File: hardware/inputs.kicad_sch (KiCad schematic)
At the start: 49 parts, among them J1 OLED_128x64

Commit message: fix switches to be correct order and move diodes
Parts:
- renumbered S15 to S13, S16 to S14, S17 to S15, S18 to S16, S13 to S17, S14 to S18
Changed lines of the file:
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@@
 		(dnp no)
 		(fields_autoplaced yes)
-		(property "Reference" "S14"
+		(property "Reference" "S18"
 			(at 220.98 62.23 0)
 			(effects
@@
 			(project "final_macropad"
 				(path "/5d184ef1-151a-4114-9d49-de87ac832ddf/ff01279d-20e0-401c-840f-7481298d2544"
-					(reference "S14")
+					(reference "S18")
 					(unit 1)
 				)
@@
 		(dnp no)
 		(fields_autoplaced yes)
-		(property "Reference" "S18"
+		(property "Reference" "S16"
 			(at 101.6 96.52 0)
 			(effects
@@
 			(project "final_macropad"
 				(path "/5d184ef1-151a-4114-9d49-de87ac832ddf/ff01279d-20e0-401c-840f-7481298d2544"
-					(reference "S18")
+					(reference "S16")
 					(unit 1)
 				)
@@
 		(dnp no)
 		(fields_autoplaced yes)
-		(property "Reference" "S15"
+		(property "Reference" "S13"
 			(at 62.23 96.52 0)
 			(effects
@@
 			(project "final_macropad"
 				(path "/5d184ef1-151a-4114-9d49-de87ac832ddf/ff01279d-20e0-401c-840f-7481298d2544"
-					(reference "S15")
+					(reference "S13")
 					(unit 1)
 				)
@@
 		(dnp no)
 		(fields_autoplaced yes)
-		(property "Reference" "S13"
+		(property "Reference" "S17"
 			(at 220.98 29.21 0)
 			(effects
@@
 			(project "final_macropad"
 				(path "/5d184ef1-151a-4114-9d49-de87ac832ddf/ff01279d-20e0-401c-840f-7481298d2544"
-					(reference "S13")
+					(reference "S17")
 					(unit 1)
 				)
@@
 		(dnp no)
 		(fields_autoplaced yes)
-		(property "Reference" "S17"
+		(property "Reference" "S15"
 			(at 87.63 96.52 0)
 			(effects
@@
 			(project "final_macropad"
 				(path "/5d184ef1-151a-4114-9d49-de87ac832ddf/ff01279d-20e0-401c-840f-7481298d2544"
-					(reference "S17")
+					(reference "S15")
 					(unit 1)
 				)
@@
 		(dnp no)
 		(fields_autoplaced yes)
-		(property "Reference" "S16"
+		(property "Reference" "S14"
 			(at 76.2 96.52 0)
 			(effects
@@
 			(project "final_macropad"
 				(path "/5d184ef1-151a-4114-9d49-de87ac832ddf/ff01279d-20e0-401c-840f-7481298d2544"
-					(reference "S16")
+					(reference "S14")
 					(unit 1)
 				)

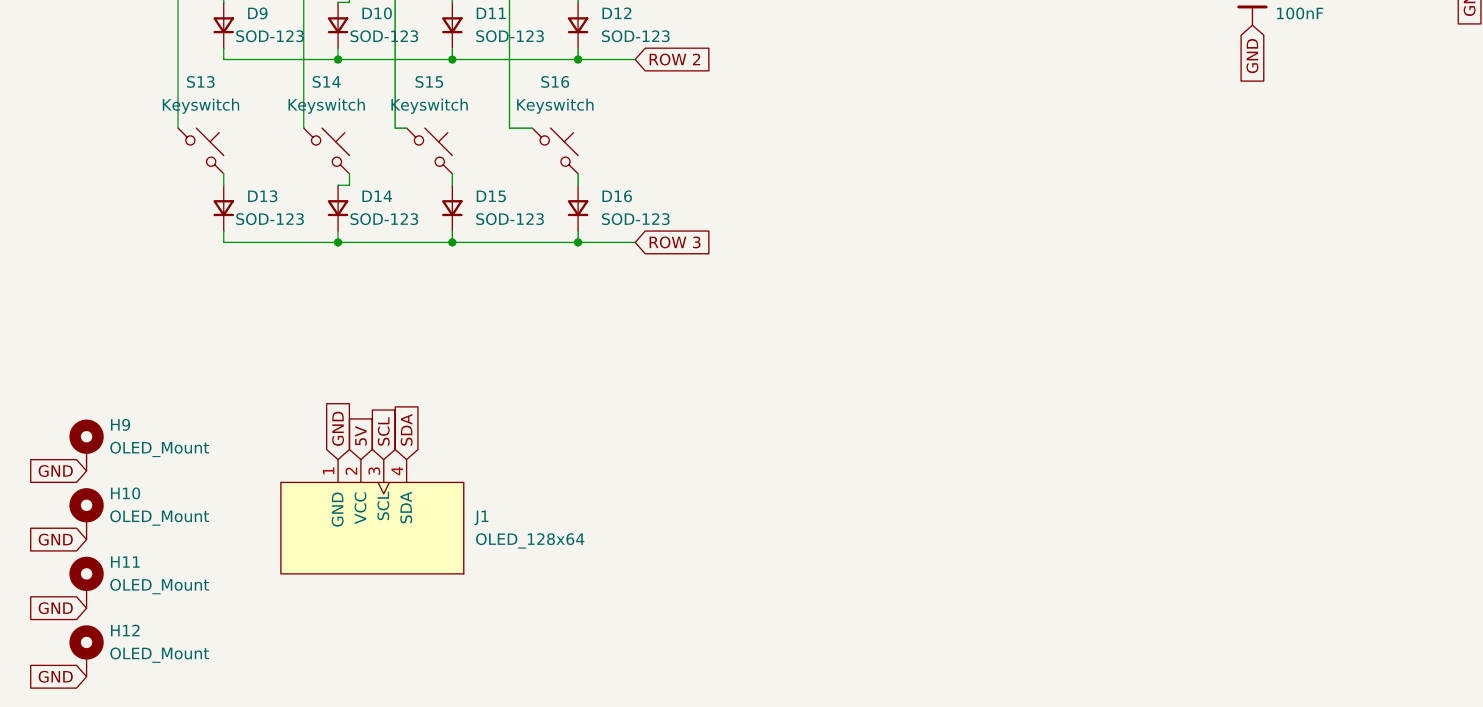
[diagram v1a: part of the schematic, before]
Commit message: route USBC connector
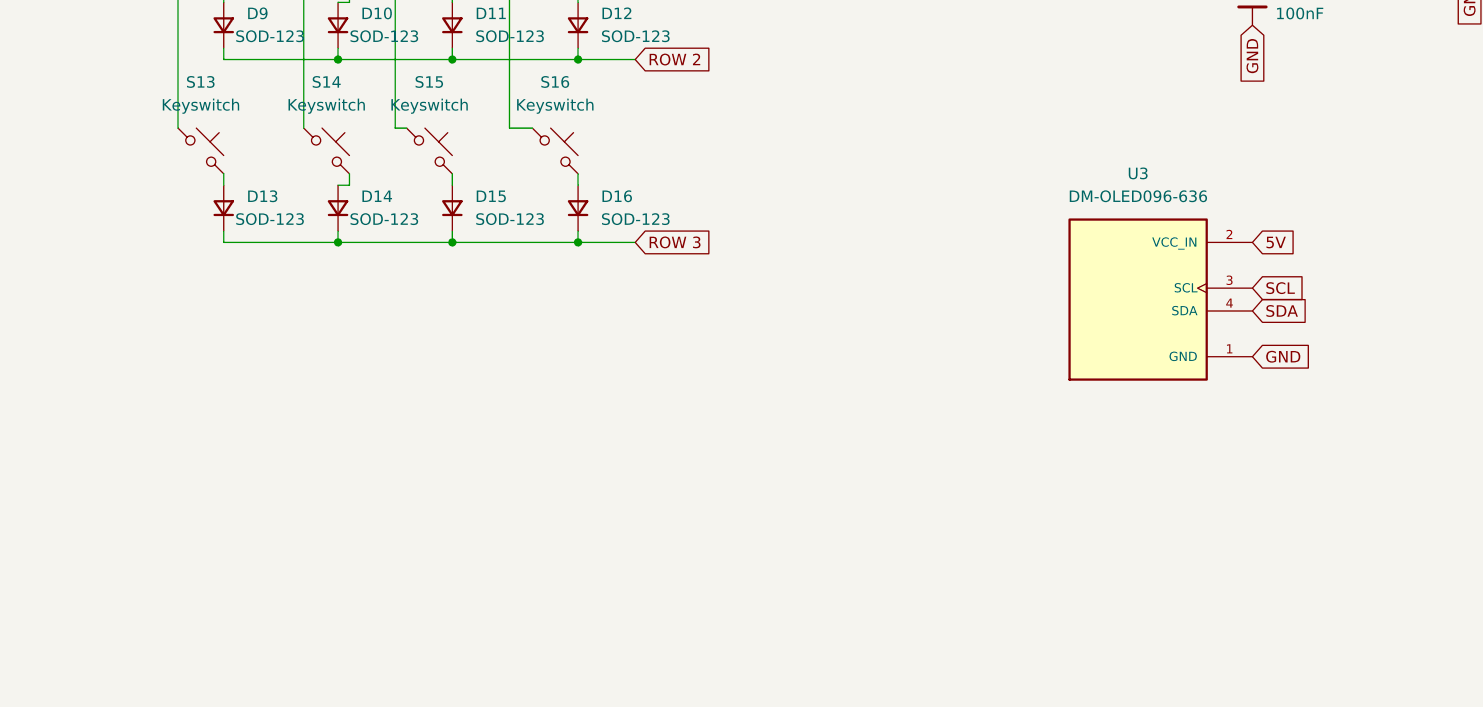
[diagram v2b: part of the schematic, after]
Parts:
- removed H10, H11, H12, H9: OLED_Mount, MountingHole:MountingHole_2.2mm_M2_Pad, symbol Mechanical:MountingHole_Pad
- removed J1: OLED_128x64, ScottoKeebs_Components:OLED_128x64, symbol ScottoKeebs:OLED_128x64
- added U3: DM-OLED096-636, kicad-footprints:MODULE_DM-OLED096-636, symbol DM-OLED096-636:DM-OLED096-636
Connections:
- net 5V: now also U3.2 (VCC_IN)
- net GND: now also U3.1 (GND)
- net SCL: now also U3.3 (SCL)
- net SDA: now also U3.4 (SDA)
